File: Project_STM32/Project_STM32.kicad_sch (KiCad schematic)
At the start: 33 parts, among them J1 Serial_Debug_Conn, J2 Conn_01x04_Pin, J3 Conn_01x04_Pin, J4 USB_C_Receptacle_USB2.0_16P, SW1 SW_SPDT, U1 STM32F405RGT6, U2 MIC5366-3.3YC5, U3 USBLC6-2SC6, Y1 16MH

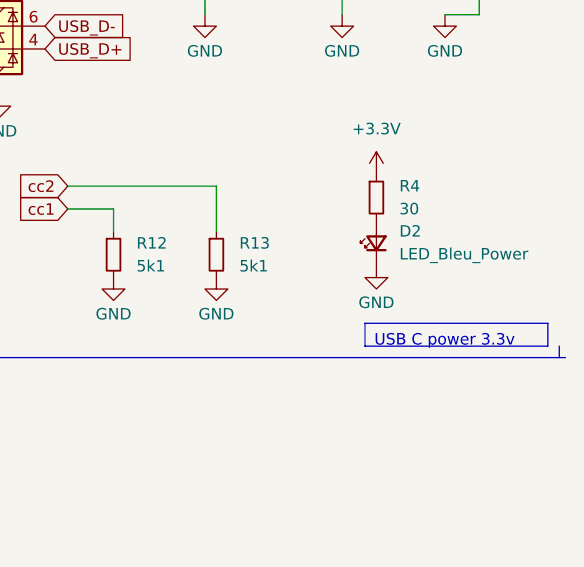
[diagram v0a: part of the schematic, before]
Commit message: added the .net file for the compnent size
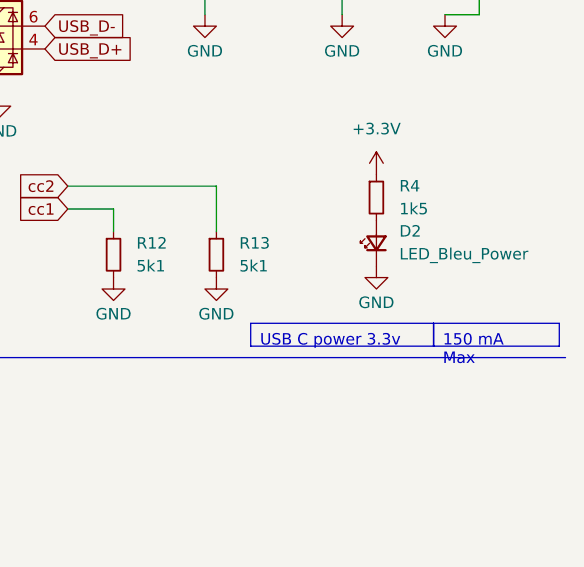
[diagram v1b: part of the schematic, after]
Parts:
- C1, C12, C13, C2, C3: footprint (none) -> Capacitor_SMD:C_0603_1608Metric
- C10, C11, C4, C5, C6, C7, C8, C9: footprint (none) -> Capacitor_SMD:C_0402_1005Metric
- D1, D2: footprint (none) -> LED_SMD:LED_0603_1608Metric
- J1: footprint (none) -> Connector_PinSocket_1.27mm:PinSocket_2x05_P1.27mm_Vertical_SMD
- J2, J3: footprint (none) -> Connector_PinHeader_1.27mm:PinHeader_1x04_P1.27mm_Vertical
- J4: footprint (none) -> Connector_USB:USB_C_Receptacle_GCT_USB4110
- L2: footprint (none) -> Inductor_SMD:L_0402_1005Metric
- R1, R10, R2, R9: footprint (none) -> Resistor_SMD:R_0402_1005Metric
- R12, R13, R3: footprint (none) -> Resistor_SMD:R_0603_1608Metric
- R4: value 30 -> 1k5; footprint (none) -> Resistor_SMD:R_0603_1608Metric
- SW1: footprint (none) -> Button_Switch_SMD:SW_SPDT_PCM12
- Y1: footprint (none) -> Crystal:Crystal_SMD_3225-4Pin_3.2x2.5mm
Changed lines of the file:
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@@
 		)
 	)
-	(polyline
-		(pts
-			(xy 284.48 76.2) (xy 284.48 74.93)
-		)
-		(stroke
-			(width 0)
-			(type default)
-		)
-	)
 	(wire
 		(pts
@@
 		)
 	)
+	(text_box "150 mA Max\n"
+		(exclude_from_sim no)
+		(at 270.51 72.39 0)
+		(size 13.97 2.54)
+		(stroke
+			(width 0)
+			(type default)
+		)
+		(fill
+			(type none)
+		)
+		(effects
+			(font
+				(size 1.27 1.27)
+			)
+			(justify left top)
+		)
+	)
 	(text_box "USB C power 3.3v\n"
 		(exclude_from_sim no)
-		(at 262.89 72.39 0)
+		(at 250.19 72.39 0)
 		(size 20.32 2.54)
 		(stroke
@@
 			)
 		)
-		(property "Value" "30"
+		(property "Value" "1k5"
 			(at 266.7 59.6899 0)
 			(effects
@@
 			)
 		)
-		(property "Footprint" ""
+		(property "Footprint" "Resistor_SMD:R_0603_1608Metric"
 			(at 264.16 58.42 0)
 			(effects
@@
 			)
 		)
-		(property "Footprint" ""
+		(property "Footprint" "Capacitor_SMD:C_0402_1005Metric"
 			(at 52.07 77.47 0)
 			(effects
@@
 			)
 		)
-		(property "Footprint" ""
+		(property "Footprint" "Connector_USB:USB_C_Receptacle_GCT_USB4110"
 			(at 199.39 39.37 0)
 			(effects
@@
 			)
 		)
-		(property "Footprint" ""
+		(property "Footprint" "Button_Switch_SMD:SW_SPDT_PCM12"
 			(at 101.6 140.97 0)
 			(effects
@@
 			)
 		)
-		(property "Footprint" ""
+		(property "Footprint" "Capacitor_SMD:C_0402_1005Metric"
 			(at 62.23 77.47 0)
 			(effects
@@
 			)
 		)
-		(property "Footprint" ""
+		(property "Footprint" "Resistor_SMD:R_0603_1608Metric"
 			(at 246.38 64.77 0)
 			(effects
@@
 			)
 		)
-		(property "Footprint" ""
+		(property "Footprint" "Resistor_SMD:R_0402_1005Metric"
 			(at 97.79 102.87 0)
 			(effects
@@
 			)
 		)
-		(property "Footprint" ""
+		(property "Footprint" "Capacitor_SMD:C_0603_1608Metric"
 			(at 275.59 29.21 0)
 			(effects
@@
 			)
 		)
-		(property "Footprint" ""
+		(property "Footprint" "Inductor_SMD:L_0402_1005Metric"
 			(at 85.09 74.93 0)
 			(effects
@@
 			)
 		)
-		(property "Footprint" ""
+		(property "Footprint" "Connector_PinHeader_1.27mm:PinHeader_1x04_P1.27mm_Vertical"
 			(at 199.39 154.94 0)
 			(effects
@@
 			)
 		)
-		(property "Footprint" ""
+		(property "Footprint" "Resistor_SMD:R_0402_1005Metric"
 			(at 105.41 102.87 0)
 			(effects
@@
 			)
 		)
-		(property "Footprint" ""
+		(property "Footprint" "Capacitor_SMD:C_0402_1005Metric"
 			(at 31.75 77.47 0)
 			(effects
@@
 			)
 		)
-		(property "Footprint" ""
+		(property "Footprint" "Resistor_SMD:R_0402_1005Metric"
 			(at 105.41 179.07 0)
 			(effects
@@
 			)
 		)
-		(property "Footprint" ""
+		(property "Footprint" "Connector_PinSocket_1.27mm:PinSocket_2x05_P1.27mm_Vertical_SMD"
 			(at 147.32 177.8 0)
 			(effects
@@
 			)
 		)
-		(property "Footprint" ""
+		(property "Footprint" "Connector_PinHeader_1.27mm:PinHeader_1x04_P1.27mm_Vertical"
 			(at 233.68 152.4 0)
 			(effects
@@
 			)
 		)
-		(property "Footprint" ""
+		(property "Footprint" "Capacitor_SMD:C_0603_1608Metric"
 			(at 20.32 77.47 0)
 			(effects
@@
 			)
 		)
-		(property "Footprint" ""
+		(property "Footprint" "Capacitor_SMD:C_0402_1005Metric"
 			(at 92.71 187.96 0)
 			(effects
@@
 			)
 		)
-		(property "Footprint" ""
+		(property "Footprint" "Resistor_SMD:R_0402_1005Metric"
 			(at 101.6 152.4 0)
 			(effects
@@
 			)
 		)
-		(property "Footprint" ""
+		(property "Footprint" "Capacitor_SMD:C_0603_1608Metric"
 			(at 25.4 172.72 0)
 			(effects
@@
 			)
 		)
-		(property "Footprint" ""
+		(property "Footprint" "Capacitor_SMD:C_0402_1005Metric"
 			(at 102.87 187.96 0)
 			(effects
@@
 			)
 		)
-		(property "Footprint" ""
+		(property "Footprint" "LED_SMD:LED_0603_1608Metric"
 			(at 17.78 142.24 90)
 			(effects
@@
 			)
 		)
-		(property "Footprint" ""
+		(property "Footprint" "Capacitor_SMD:C_0603_1608Metric"
 			(at 17.78 172.72 0)
 			(effects
@@
 			)
 		)
-		(property "Footprint" ""
+		(property "Footprint" "Capacitor_SMD:C_0402_1005Metric"
 			(at 88.9 78.74 0)
 			(effects
@@
 			)
 		)
-		(property "Footprint" ""
+		(property "Footprint" "LED_SMD:LED_0603_1608Metric"
 			(at 264.16 63.5 90)
 			(effects
@@
 			)
 		)
-		(property "Footprint" ""
+		(property "Footprint" "Capacitor_SMD:C_0603_1608Metric"
 			(at 241.3 31.75 0)
 			(effects
@@
 			)
 		)
-		(property "Footprint" ""
+		(property "Footprint" "Resistor_SMD:R_0603_1608Metric"
 			(at 234.95 64.77 0)
 			(effects
@@
 			)
 		)
-		(property "Footprint" ""
+		(property "Footprint" "Capacitor_SMD:C_0402_1005Metric"
 			(at 41.91 77.47 0)
 			(effects
@@
 			)
 		)
-		(property "Footprint" ""
+		(property "Footprint" "Capacitor_SMD:C_0402_1005Metric"
 			(at 99.06 78.74 0)
 			(effects
@@
 			)
 		)
-		(property "Footprint" ""
+		(property "Footprint" "Crystal:Crystal_SMD_3225-4Pin_3.2x2.5mm"
 			(at 97.79 182.88 0)
 			(effects
@@
 			)
 		)
-		(property "Footprint" ""
+		(property "Footprint" "Resistor_SMD:R_0603_1608Metric"
 			(at 17.78 149.86 0)
 			(effects

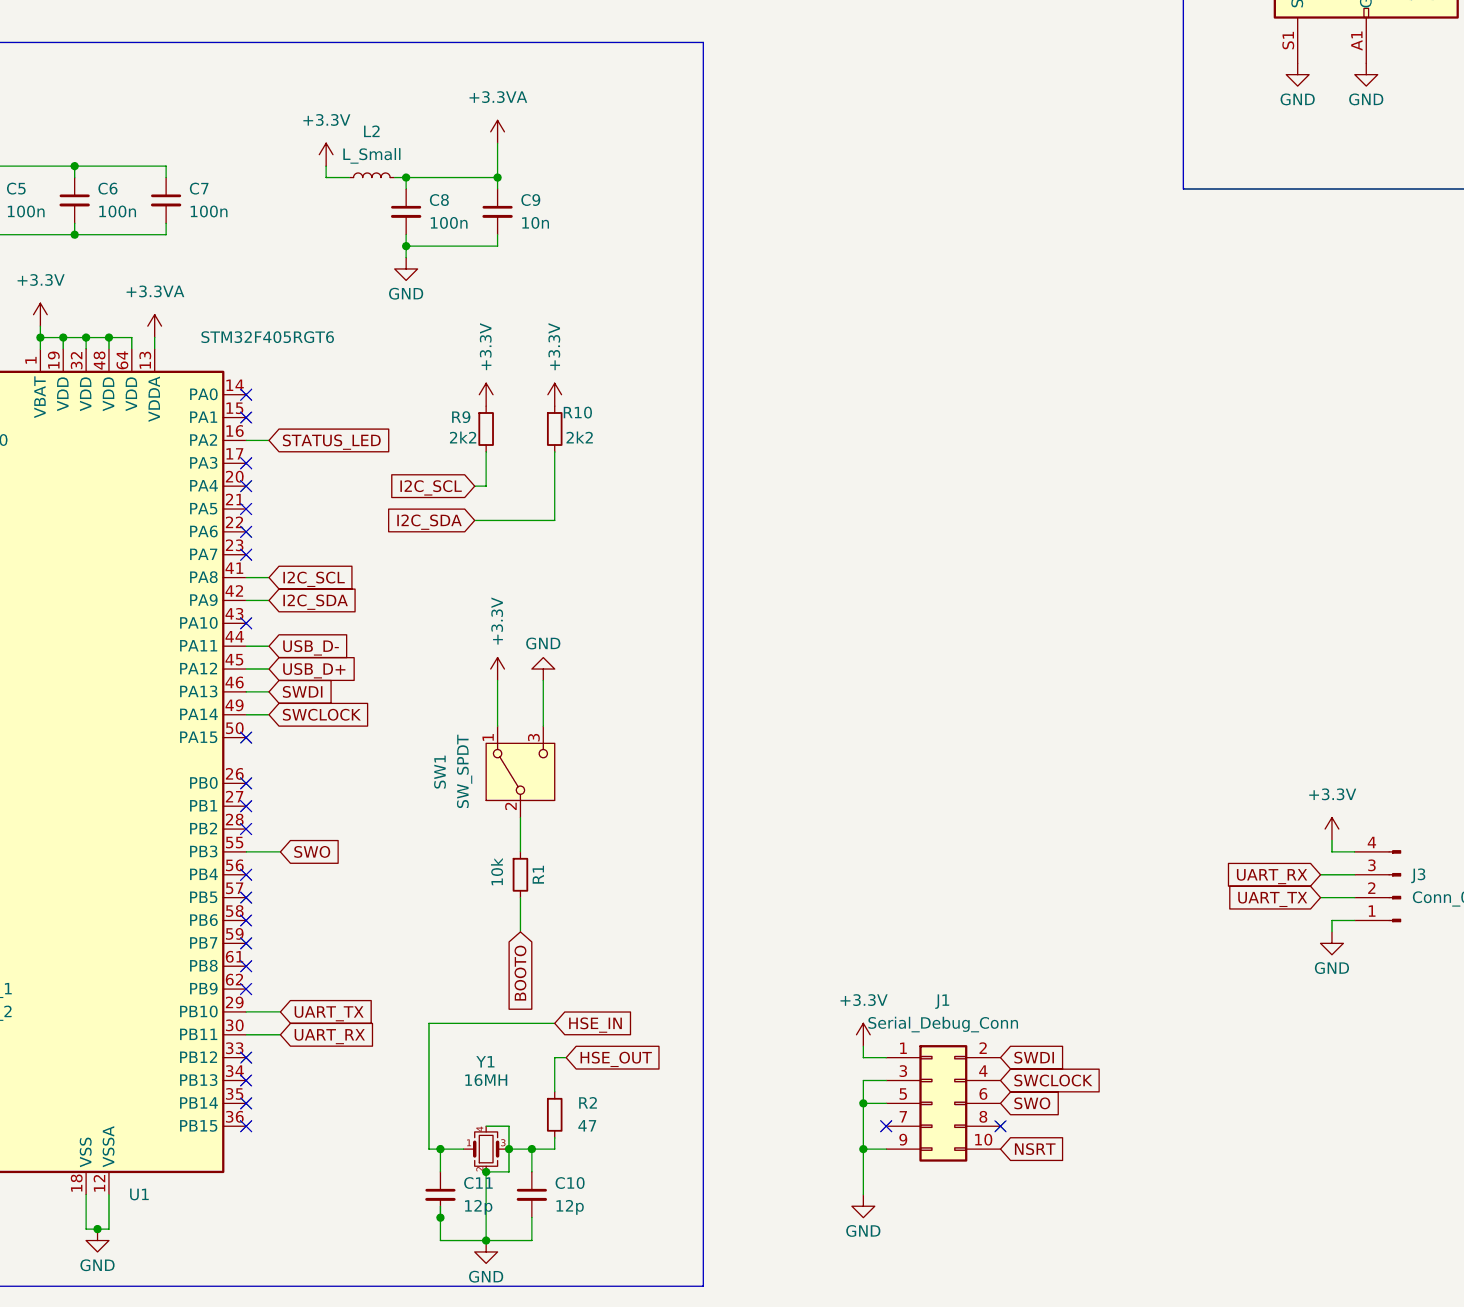
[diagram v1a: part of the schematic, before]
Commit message: general shape of the board done, fix small issues
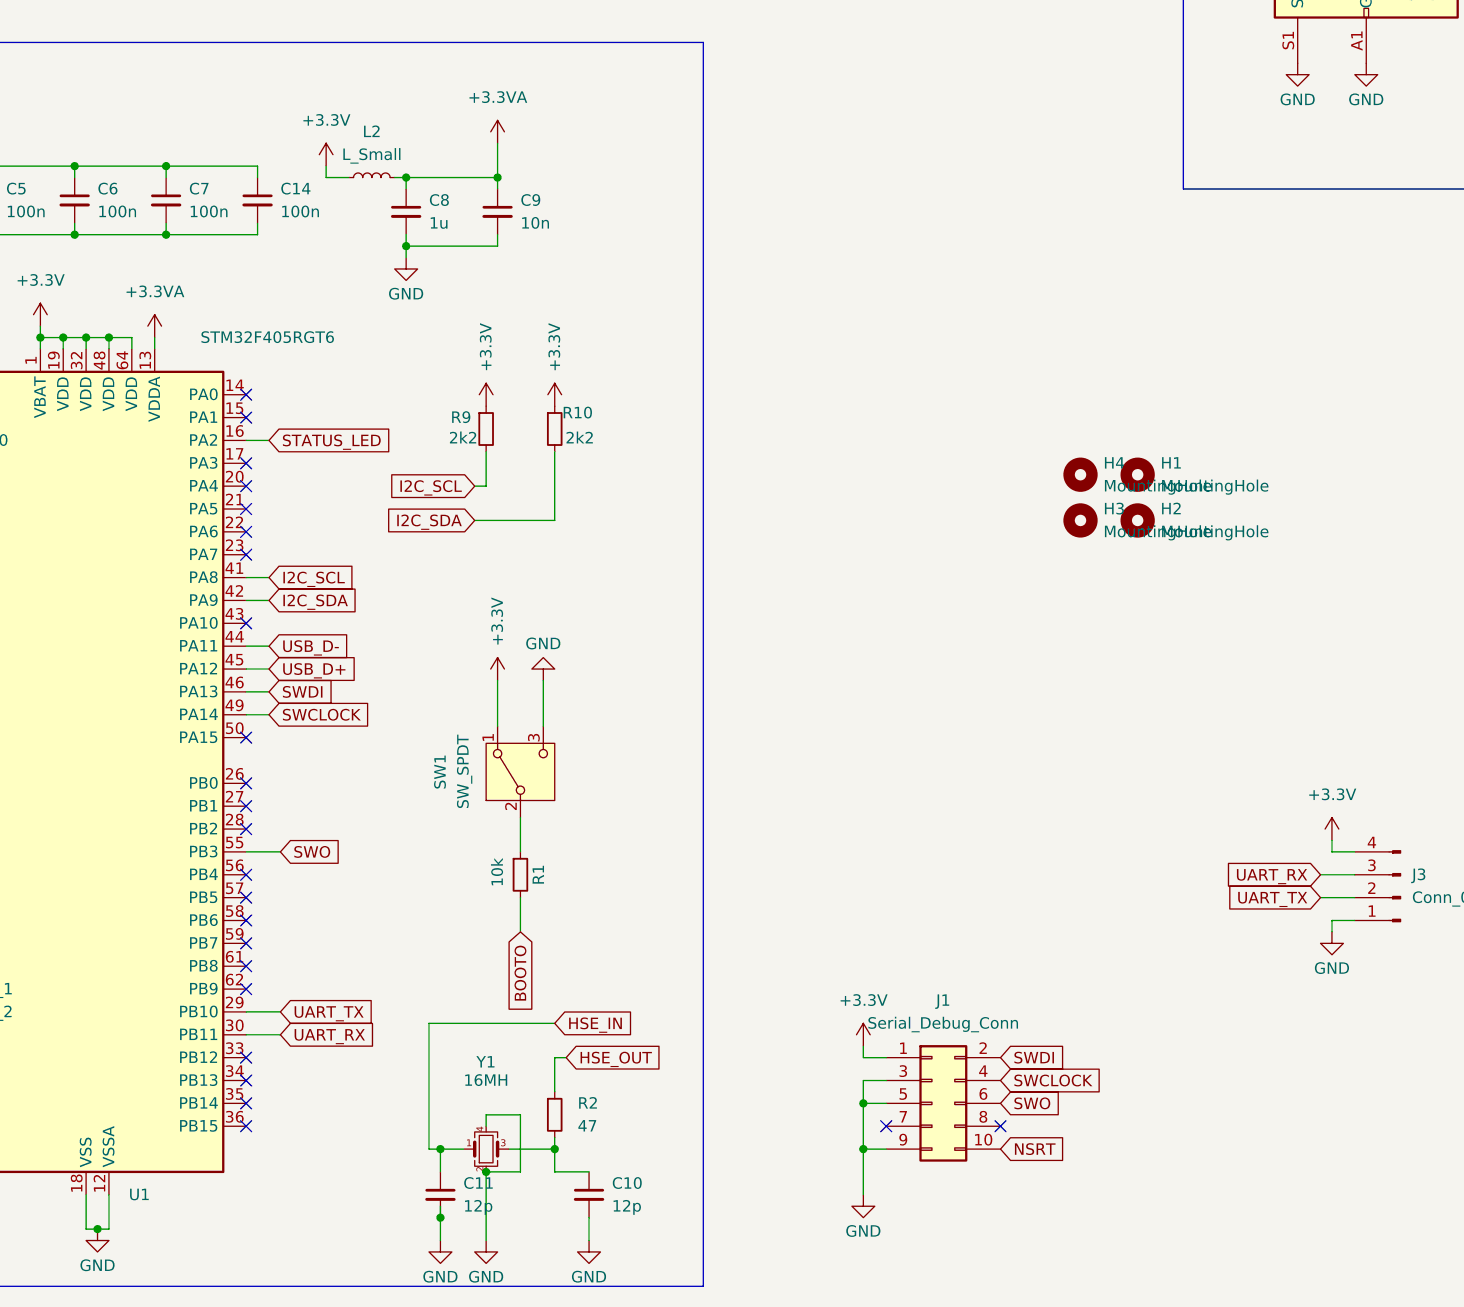
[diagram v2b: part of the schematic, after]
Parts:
- added C14: 100n, Capacitor_SMD:C_0402_1005Metric, symbol Device:C_Small
- added H1, H2, H3, H4: MountingHole, MountingHole:MountingHole_3.2mm_M3, symbol Mechanical:MountingHole
- C8: value 100n -> 1u
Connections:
- net +3.3V: now also C14.1
- net GND: now also C14.2; no longer C10.1, R2.2, Y1.3
- new net: C10.1, R2.2, Y1.3
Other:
- moved on the sheet: C10
